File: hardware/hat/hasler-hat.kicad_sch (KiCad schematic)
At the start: 116 parts, among them J1 Amp4 top header, J2 Hasler J2, J3 USB-C PD in, J4 Debug / expansion, J5 Qwiic, J6 To Amp4 DC in, U1 MCP23017, U10 SRV05-4, U11 SRV05-4, U12 SRV05-4, U2 ADS1115, U3 CH224A, U4 TPS259474ARPWR, U6 XC6206P332MR, U7 SRV05-4, U8 SRV05-4, U9 SRV05-4

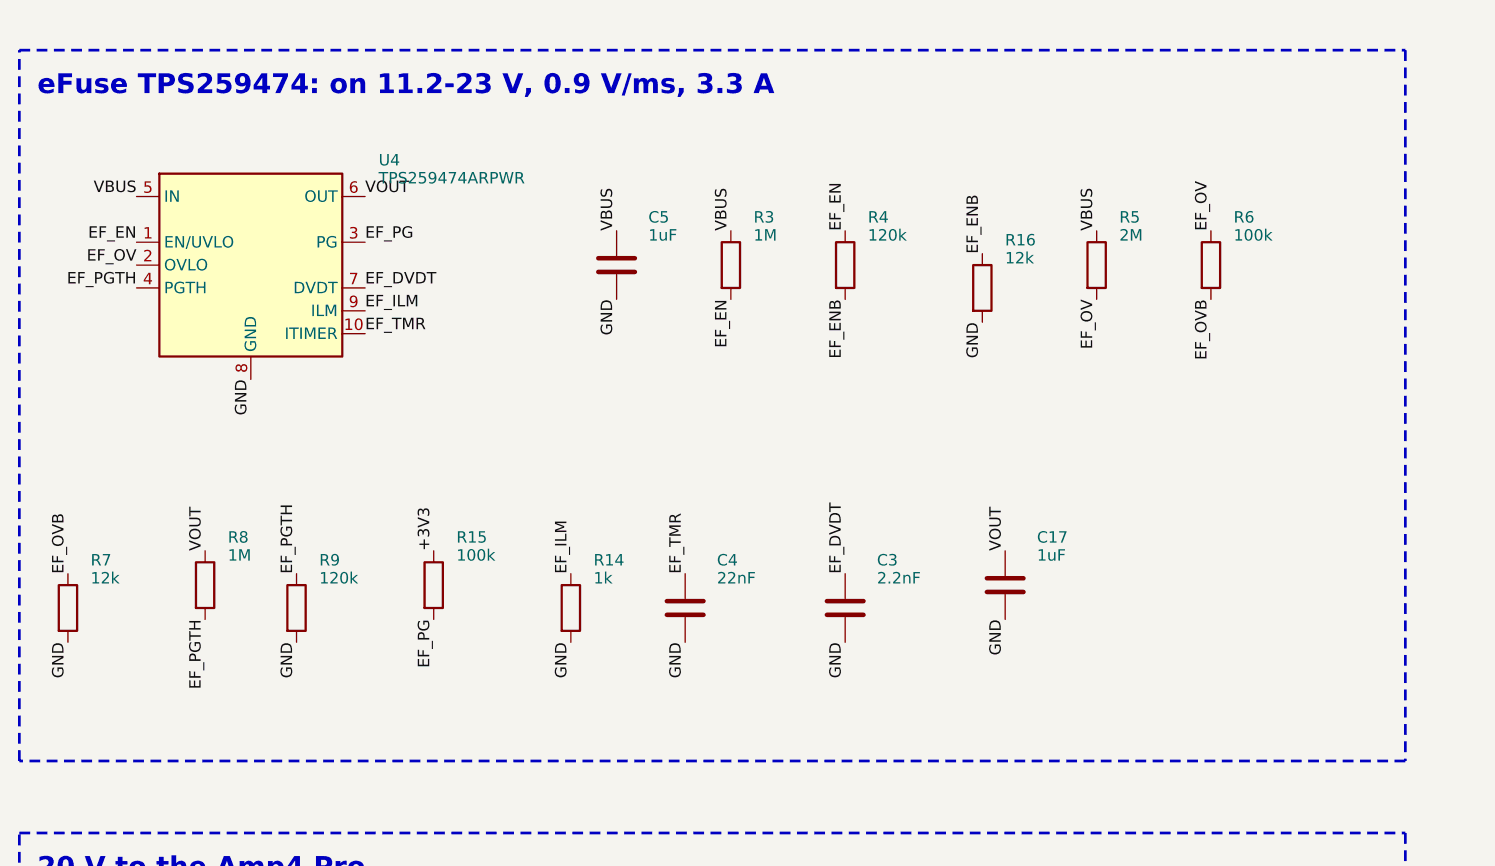
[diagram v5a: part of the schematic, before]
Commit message: HAT: eFuse turns on at the charger's 5 V (JP11 for 10.3 V), CH224A cap under the chip, review round 4
A start-up model with the Amp4's measured 220 uF and the Pi booting part-way up the
ramp showed the eFuse could overheat and restart for ever with a 10.3 V UVLO, at any
ramp rate. With JP11 open (as shipped) EN is pulled up by R3 alone, so U4 is fully
on before the PD contract and the 5 -> 20 V step costs it nothing; bridging JP11
restores the 10.3 V UVLO. C1 moved right under the CH224A (was ~20 mm of copper away).
In2 links for 3V3A (C41-C42), ADS_RDY and SDA. Bottom silk: eFuse line fixed,
JLC placeholder removed, an easter egg. Zip without the job file and drill maps.
check.py (fast netlist/BOM/threshold check, run by build.sh). Docs: start-up
analysis, 3V3A current limit, bring-up, edge rails, round-4 review. Renders without C7.

Co-Authored-By: Claude Opus 5.5 <noreply@anthropic.com>
Claude-Session: https://claude.ai/code/session_014wovV18Ypx4LXt9k8BSCRk
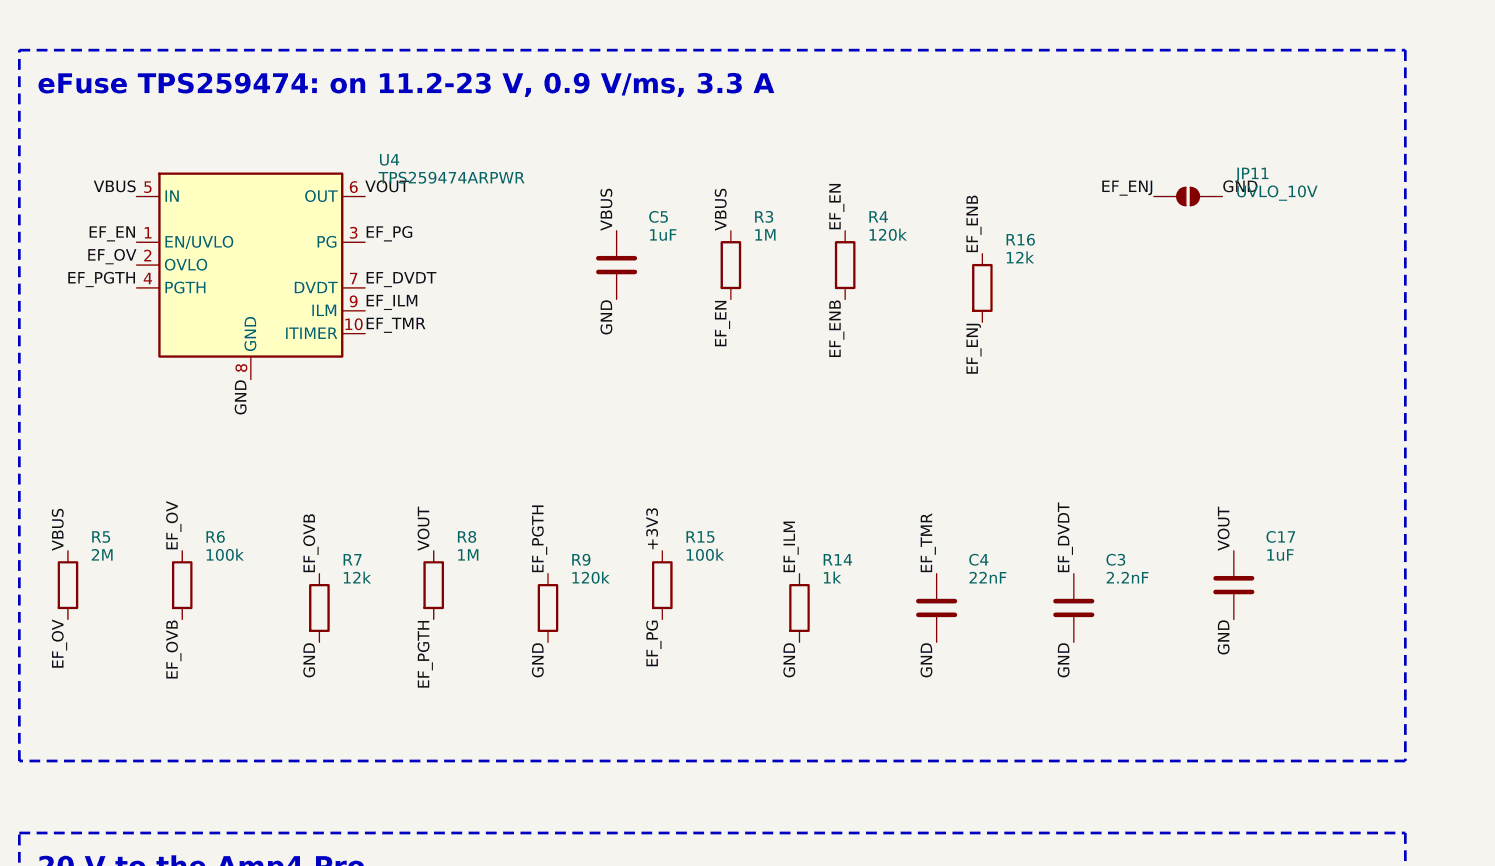
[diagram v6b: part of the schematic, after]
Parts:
- added JP11: UVLO_10V, Jumper:SolderJumper-2_P1.3mm_Open_RoundedPad1.0x1.5mm, symbol Jumper:SolderJumper_2_Open
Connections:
- net GND: now also JP11.2 (B); no longer R16.2
- new net EF_ENJ: JP11.1 (A), R16.2
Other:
- moved on the sheet: C17, C3, C4, R14, R15, R5, R6, R7, R8, R9

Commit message: HAT: J6 on a KF350 footprint so its orientation is unambiguous
JLC asked whether J6 faced the right way: the Phoenix PT-1,5 outline did not
match the KF350 they fit. New generated footprint (make_fp.py) keeps the
Phoenix pads exactly (pin 1 at the origin, 1.2/2.4 mm) and draws the KF350
body with the wire openings on the edge side.

Swapped in place on the board (same position, nets, fields, pad UUIDs), so
copper and routing are untouched: only F.Silkscreen changes in the Gerbers;
CPL identical, BOM footprint name only. DRC (all severities, schematic
parity) and ERC clean.

Co-Authored-By: Claude Opus 5.5 <noreply@anthropic.com>
Claude-Session: https://claude.ai/code/session_014wovV18Ypx4LXt9k8BSCRk
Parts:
- J6: footprint TerminalBlock_Phoenix:TerminalBlock_Phoenix_PT-1,5-2-3.5-H_1x02_P3.50mm_Horizontal -> hasler:TerminalBlock_Kefa_KF350-3.5-2P_1x02_P3.50mm_Horizontal
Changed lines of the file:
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@@
 			)
 		)
-		(property "Footprint" "TerminalBlock_Phoenix:TerminalBlock_Phoenix_PT-1,5-2-3.5-H_1x02_P3.50mm_Horizontal"
+		(property "Footprint" "hasler:TerminalBlock_Kefa_KF350-3.5-2P_1x02_P3.50mm_Horizontal"
 			(at 139.7 246.38 0)
 			(effects
